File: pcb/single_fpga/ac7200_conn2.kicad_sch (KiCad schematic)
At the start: 1 part, among them U97 ALINX AC7200 (XC7A200T-2FBG48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

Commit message: Changed position.
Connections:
- net GND: now also U97.CON2_10 (GND), U97.CON2_19 (GND), U97.CON2_20 (GND), U97.CON2_29 (GND), U97.CON2_30 (GND), U97.CON2_39 (GND), U97.CON2_40 (GND), U97.CON2_49 (GND), U97.CON2_50 (GND), U97.CON2_59 (GND), U97.CON2_60 (GND), U97.CON2_69 (GND), U97.CON2_70 (GND), U97.CON2_9 (GND)

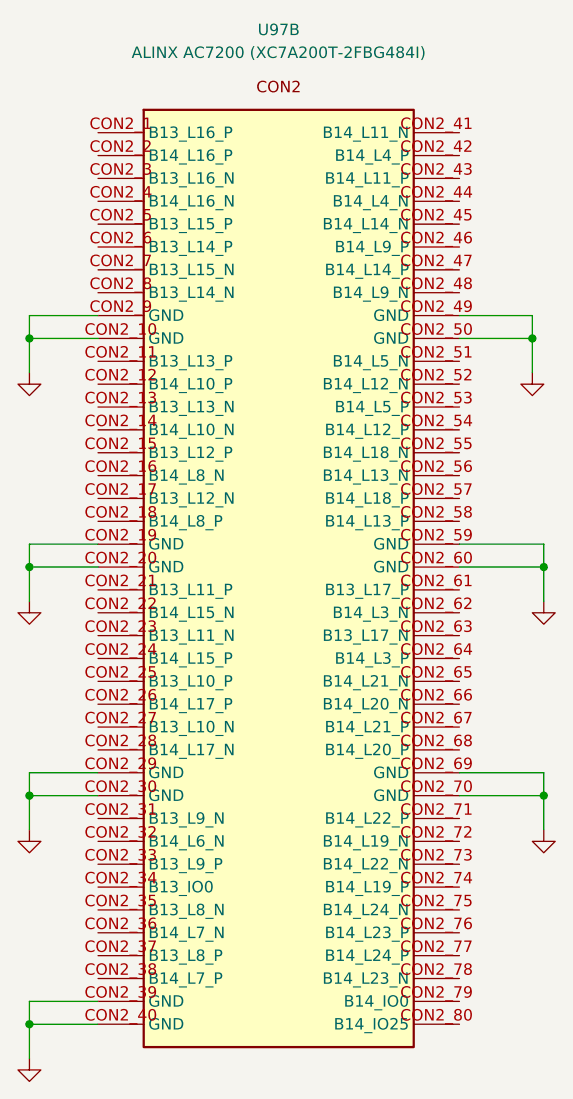
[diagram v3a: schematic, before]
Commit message: Reorganized sheets for two-boards. Fixed connector off-grid problems.
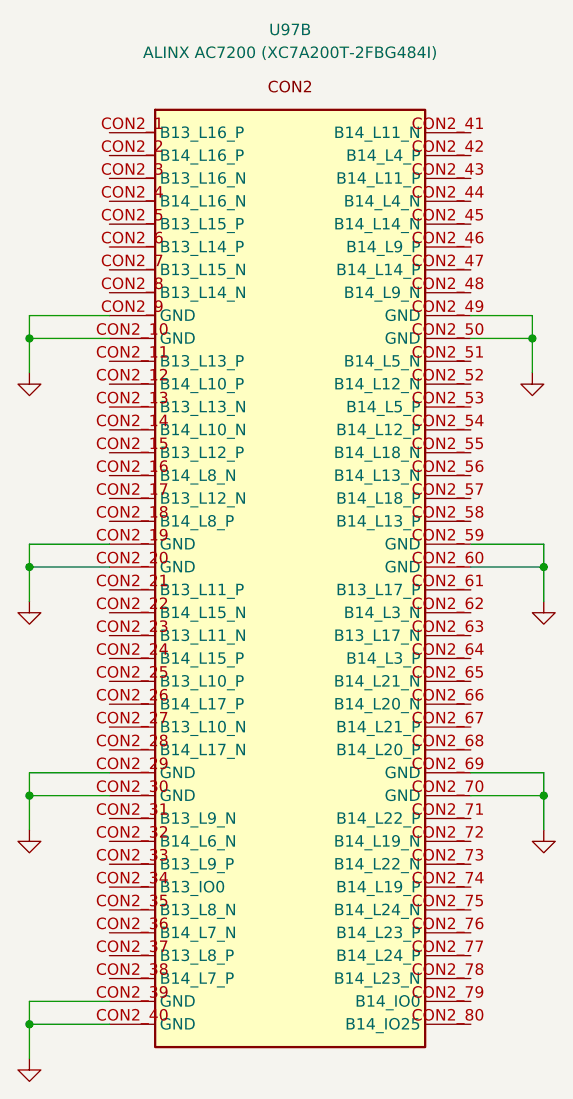
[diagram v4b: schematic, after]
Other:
- moved on the sheet: U97B
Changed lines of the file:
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@@
 	(paper "A4")
+	(junction
+		(at 114.3 101.6)
+		(diameter 0)
+		(color 0 0 0 0)
+	)
 	(junction
 		(at 114.3 127)
@@
 	)
 	(junction
-		(at 114.3 76.2)
+		(at 114.3 152.4)
 		(diameter 0)
 		(color 0 0 0 0)
@@
 	)
 	(junction
-		(at 114.3 152.4)
+		(at 170.18 76.2)
 		(diameter 0)
 		(color 0 0 0 0)
@@
 	)
 	(junction
-		(at 114.3 101.6)
+		(at 114.3 76.2)
 		(diameter 0)
 		(color 0 0 0 0)
 	)
-	(junction
-		(at 170.18 76.2)
-		(diameter 0)
-		(color 0 0 0 0)
-	)
-	(wire
-		(pts
-			(xy 162.08 101.6) (xy 171.45 101.6)
-		)
-		(stroke
-			(width 0)
-			(type default)
-		)
-	)
-	(wire
-		(pts
-			(xy 114.3 76.2) (xy 121.92 76.2)
-		)
-		(stroke
-			(width 0)
-			(type default)
-		)
-	)
-	(wire
-		(pts
-			(xy 162.08 73.66) (xy 170.18 73.66)
+	(wire
+		(pts
+			(xy 163.35 101.6) (xy 171.45 101.6)
+		)
+		(stroke
+			(width 0)
+			(type default)
+		)
+	)
+	(wire
+		(pts
+			(xy 114.3 76.2) (xy 123.19 76.2)
+		)
+		(stroke
+			(width 0)
+			(type default)
+		)
+	)
+	(wire
+		(pts
+			(xy 163.35 73.66) (xy 170.18 73.66)
 		)
 		(stroke
@@
 	(wire
 		(pts
-			(xy 114.3 99.06) (xy 121.92 99.06)
-		)
-		(stroke
-			(width 0)
-			(type default)
-		)
-	)
-	(wire
-		(pts
-			(xy 114.3 152.4) (xy 121.92 152.4)
+			(xy 114.3 99.06) (xy 123.19 99.06)
+		)
+		(stroke
+			(width 0)
+			(type default)
+		)
+	)
+	(wire
+		(pts
+			(xy 114.3 152.4) (xy 123.19 152.4)
 		)
 		(stroke
@@
 	(wire
 		(pts
-			(xy 162.08 124.46) (xy 171.45 124.46)
-		)
-		(stroke
-			(width 0)
-			(type default)
-		)
-	)
-	(wire
-		(pts
-			(xy 114.3 127) (xy 121.92 127)
-		)
-		(stroke
-			(width 0)
-			(type default)
-		)
-	)
-	(wire
-		(pts
-			(xy 162.08 99.06) (xy 171.45 99.06)
-		)
-		(stroke
-			(width 0)
-			(type default)
-		)
-	)
-	(wire
-		(pts
-			(xy 162.08 127) (xy 171.45 127)
+			(xy 163.35 124.46) (xy 171.45 124.46)
+		)
+		(stroke
+			(width 0)
+			(type default)
+		)
+	)
+	(wire
+		(pts
+			(xy 114.3 127) (xy 123.19 127)
+		)
+		(stroke
+			(width 0)
+			(type default)
+		)
+	)
+	(wire
+		(pts
+			(xy 163.35 99.06) (xy 171.45 99.06)
+		)
+		(stroke
+			(width 0)
+			(type default)
+		)
+	)
+	(wire
+		(pts
+			(xy 163.35 127) (xy 171.45 127)
 		)
 		(stroke
@@
 	(wire
 		(pts
-			(xy 114.3 73.66) (xy 121.92 73.66)
+			(xy 114.3 73.66) (xy 123.19 73.66)
 		)
 		(stroke
@@
 	(wire
 		(pts
-			(xy 114.3 149.86) (xy 121.92 149.86)
+			(xy 114.3 149.86) (xy 123.19 149.86)
 		)
 		(stroke
@@
 	(wire
 		(pts
-			(xy 162.08 76.2) (xy 170.18 76.2)
-		)
-		(stroke
-			(width 0)
-			(type default)
-		)
-	)
-	(wire
-		(pts
-			(xy 114.3 124.46) (xy 121.92 124.46)
+			(xy 163.35 76.2) (xy 170.18 76.2)
+		)
+		(stroke
+			(width 0)
+			(type default)
+		)
+	)
+	(wire
+		(pts
+			(xy 114.3 124.46) (xy 123.19 124.46)
 		)
 		(stroke
@@
 	(wire
 		(pts
-			(xy 114.3 101.6) (xy 121.92 101.6)
+			(xy 114.3 101.6) (xy 123.19 101.6)
 		)
 		(stroke
@@
 		(dnp no)
 		(fields_autoplaced yes)
-		(property "Reference" "#PWR009"
+		(property "Reference" "#PWR09"
 			(at 114.3 86.36 0)
 			(hide yes)
@@
 		(instances
 			(project "top"
-				(path "/12638caa-1907-413e-8e98-06abbbf6ccbc/d4107e22-3cf2-453c-a22c-8e2acaca2e5b/b8c40ea9-0d6a-4a7f-8d5e-85c23412f0d2"
-					(reference "#PWR009")
+				(path "/12638caa-1907-413e-8e98-06abbbf6ccbc/8ee3463b-0816-4e24-be6c-9811f4c49ad3/32c479b8-4af5-4d07-9387-f6769afc9e03"
+					(reference "#PWR09")
 					(unit 1)
 				)
@@
 	(symbol
 		(lib_id "single_fpga:AC7200")
-		(at 142 102.87 0)
+		(at 143.27 102.87 0)
 		(unit 2)
 		(body_style 1)
@@
 		(fields_autoplaced yes)
 		(property "Reference" "U97"
-			(at 142 41.91 0)
+			(at 143.27 41.91 0)
 			(show_name no)
 			(do_not_autoplace no)
@@
 		)
 		(property "Value" "ALINX AC7200 (XC7A200T-2FBG484I)"
-			(at 142 44.45 0)
+			(at 143.27 44.45 0)
 			(show_name no)
 			(do_not_autoplace no)
@@
 		)
 		(property "Footprint" "single_fpga:AC7200"
-			(at 142 102.87 0)
+			(at 143.27 102.87 0)
 			(hide yes)
 			(show_name no)
@@
 		)
 		(property "Datasheet" "docs/AC7200_User_Manual.pdf"
-			(at 142 102.87 0)
+			(at 143.27 102.87 0)
 			(hide yes)
 			(show_name no)
@@
 		)
 		(property "Description" "ALINX AC7200 XC7A200T-2FBG484I Artix-7 FPGA SOM, 45x55mm, 4x 80-pin/0.5mm B2B connectors (Unit A=CON1 VCCIN/GND+BANK34+BANK13+XADC, Unit B=CON2 BANK13+BANK14, Unit C=CON3 BANK15+BANK16+JTAG (TCK/TDI/TDO/TMS on pins 77-80 -- a SEPARATE on-module 6-pin JTAG header J1 also exists, not modeled here), Unit D=CON4 BANK16+GTP transceivers). Every pin cross-checked against ALINX's own real user manual (docs/AC7200_User_Manual.pdf) -- CON2/CON3/CON4 and CON1 pins 1-72 matched an earlier web-transcription exactly; CON1 pins 73-80 (previously unverified placeholder) now filled in from the real manual. ONE correction applied: CON1 pin 27 is printed as 'B13_L7_P' in ALINX's own manual (same as pin 25) -- a real duplicate/typo in their document (different FPGA balls AB11 vs AB12, and every other one of the 320 pins alternates P/N without exception) -- corrected here to B13_L7_N. Module standalone-power (J3, 2-pin +5V/GND) and JTAG (J1, 6-pin) headers exist on the module but are not part of this symbol (carrier-board-facing CON1-4 only)."
-			(at 142 102.87 0)
+			(at 143.27 102.87 0)
 			(hide yes)
 			(show_name no)
@@
 		(instances
 			(project "top"
-				(path "/12638caa-1907-413e-8e98-06abbbf6ccbc/d4107e22-3cf2-453c-a22c-8e2acaca2e5b/b8c40ea9-0d6a-4a7f-8d5e-85c23412f0d2"
+				(path "/12638caa-1907-413e-8e98-06abbbf6ccbc/8ee3463b-0816-4e24-be6c-9811f4c49ad3/32c479b8-4af5-4d07-9387-f6769afc9e03"
 					(reference "U97")
 					(unit 2)
@@
 		(instances
 			(project "top"
-				(path "/12638caa-1907-413e-8e98-06abbbf6ccbc/d4107e22-3cf2-453c-a22c-8e2acaca2e5b/b8c40ea9-0d6a-4a7f-8d5e-85c23412f0d2"
+				(path "/12638caa-1907-413e-8e98-06abbbf6ccbc/8ee3463b-0816-4e24-be6c-9811f4c49ad3/32c479b8-4af5-4d07-9387-f6769afc9e03"
 					(reference "#PWR010")
 					(unit 1)
@@
 		(instances
 			(project "top"
-				(path "/12638caa-1907-413e-8e98-06abbbf6ccbc/d4107e22-3cf2-453c-a22c-8e2acaca2e5b/b8c40ea9-0d6a-4a7f-8d5e-85c23412f0d2"
+				(path "/12638caa-1907-413e-8e98-06abbbf6ccbc/8ee3463b-0816-4e24-be6c-9811f4c49ad3/32c479b8-4af5-4d07-9387-f6769afc9e03"
 					(reference "#PWR011")
 					(unit 1)
@@
 		(instances
 			(project "top"
-				(path "/12638caa-1907-413e-8e98-06abbbf6ccbc/d4107e22-3cf2-453c-a22c-8e2acaca2e5b/b8c40ea9-0d6a-4a7f-8d5e-85c23412f0d2"
+				(path "/12638caa-1907-413e-8e98-06abbbf6ccbc/8ee3463b-0816-4e24-be6c-9811f4c49ad3/32c479b8-4af5-4d07-9387-f6769afc9e03"
 					(reference "#PWR012")
 					(unit 1)
@@
 		(instances
 			(project "top"
-				(path "/12638caa-1907-413e-8e98-06abbbf6ccbc/d4107e22-3cf2-453c-a22c-8e2acaca2e5b/b8c40ea9-0d6a-4a7f-8d5e-85c23412f0d2"
+				(path "/12638caa-1907-413e-8e98-06abbbf6ccbc/8ee3463b-0816-4e24-be6c-9811f4c49ad3/32c479b8-4af5-4d07-9387-f6769afc9e03"
 					(reference "#PWR013")
 					(unit 1)
@@
 		(instances
 			(project "top"
-				(path "/12638caa-1907-413e-8e98-06abbbf6ccbc/d4107e22-3cf2-453c-a22c-8e2acaca2e5b/b8c40ea9-0d6a-4a7f-8d5e-85c23412f0d2"
+				(path "/12638caa-1907-413e-8e98-06abbbf6ccbc/8ee3463b-0816-4e24-be6c-9811f4c49ad3/32c479b8-4af5-4d07-9387-f6769afc9e03"
 					(reference "#PWR014")
 					(unit 1)
@@
 		(instances
 			(project "top"
-				(path "/12638caa-1907-413e-8e98-06abbbf6ccbc/d4107e22-3cf2-453c-a22c-8e2acaca2e5b/b8c40ea9-0d6a-4a7f-8d5e-85c23412f0d2"
+				(path "/12638caa-1907-413e-8e98-06abbbf6ccbc/8ee3463b-0816-4e24-be6c-9811f4c49ad3/32c479b8-4af5-4d07-9387-f6769afc9e03"
 					(reference "#PWR015")
 					(unit 1)

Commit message: Fixed another off-grid issue. Connected power and DATA_?? pins to inter-board connector.
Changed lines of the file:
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@@
 	(wire
 		(pts
-			(xy 163.35 101.6) (xy 171.45 101.6)
+			(xy 163.83 76.2) (xy 170.18 76.2)
 		)
 		(stroke
@@
 	(wire
 		(pts
-			(xy 163.35 73.66) (xy 170.18 73.66)
+			(xy 163.83 99.06) (xy 171.45 99.06)
 		)
 		(stroke
@@
 	(wire
 		(pts
+			(xy 163.83 73.66) (xy 170.18 73.66)
+		)
+		(stroke
+			(width 0)
+			(type default)
+		)
+	)
+	(wire
+		(pts
 			(xy 114.3 99.06) (xy 114.3 101.6)
 		)
@@
 	(wire
 		(pts
+			(xy 163.83 124.46) (xy 171.45 124.46)
+		)
+		(stroke
+			(width 0)
+			(type default)
+		)
+	)
+	(wire
+		(pts
 			(xy 114.3 152.4) (xy 123.19 152.4)
 		)
@@
 	(wire
 		(pts
-			(xy 163.35 124.46) (xy 171.45 124.46)
-		)
-		(stroke
-			(width 0)
-			(type default)
-		)
-	)
-	(wire
-		(pts
 			(xy 114.3 127) (xy 123.19 127)
 		)
@@
 	(wire
 		(pts
-			(xy 163.35 99.06) (xy 171.45 99.06)
-		)
-		(stroke
-			(width 0)
-			(type default)
-		)
-	)
-	(wire
-		(pts
-			(xy 163.35 127) (xy 171.45 127)
-		)
-		(stroke
-			(width 0)
-			(type default)
-		)
-	)
-	(wire
-		(pts
 			(xy 171.45 127) (xy 171.45 130.81)
 		)
@@
 	(wire
 		(pts
+			(xy 163.83 101.6) (xy 171.45 101.6)
+		)
+		(stroke
+			(width 0)
+			(type default)
+		)
+	)
+	(wire
+		(pts
+			(xy 163.83 127) (xy 171.45 127)
+		)
+		(stroke
+			(width 0)
+			(type default)
+		)
+	)
+	(wire
+		(pts
 			(xy 171.45 124.46) (xy 171.45 127)
-		)
-		(stroke
-			(width 0)
-			(type default)
-		)
-	)
-	(wire
-		(pts
-			(xy 163.35 76.2) (xy 170.18 76.2)
 		)
 		(stroke
@@
 	(symbol
 		(lib_id "single_fpga:AC7200")
-		(at 143.27 102.87 0)
+		(at 143.51 102.87 0)
 		(unit 2)
 		(body_style 1)
@@
 		(fields_autoplaced yes)
 		(property "Reference" "U97"
-			(at 143.27 41.91 0)
+			(at 143.51 41.91 0)
 			(show_name no)
 			(do_not_autoplace no)
@@
 		)
 		(property "Value" "ALINX AC7200 (XC7A200T-2FBG484I)"
-			(at 143.27 44.45 0)
+			(at 143.51 44.45 0)
 			(show_name no)
 			(do_not_autoplace no)
@@
 		)
 		(property "Footprint" "single_fpga:AC7200"
-			(at 143.27 102.87 0)
+			(at 143.51 102.87 0)
 			(hide yes)
 			(show_name no)
@@
 		)
 		(property "Datasheet" "docs/AC7200_User_Manual.pdf"
-			(at 143.27 102.87 0)
+			(at 143.51 102.87 0)
 			(hide yes)
 			(show_name no)
@@
 		)
 		(property "Description" "ALINX AC7200 XC7A200T-2FBG484I Artix-7 FPGA SOM, 45x55mm, 4x 80-pin/0.5mm B2B connectors (Unit A=CON1 VCCIN/GND+BANK34+BANK13+XADC, Unit B=CON2 BANK13+BANK14, Unit C=CON3 BANK15+BANK16+JTAG (TCK/TDI/TDO/TMS on pins 77-80 -- a SEPARATE on-module 6-pin JTAG header J1 also exists, not modeled here), Unit D=CON4 BANK16+GTP transceivers). Every pin cross-checked against ALINX's own real user manual (docs/AC7200_User_Manual.pdf) -- CON2/CON3/CON4 and CON1 pins 1-72 matched an earlier web-transcription exactly; CON1 pins 73-80 (previously unverified placeholder) now filled in from the real manual. ONE correction applied: CON1 pin 27 is printed as 'B13_L7_P' in ALINX's own manual (same as pin 25) -- a real duplicate/typo in their document (different FPGA balls AB11 vs AB12, and every other one of the 320 pins alternates P/N without exception) -- corrected here to B13_L7_N. Module standalone-power (J3, 2-pin +5V/GND) and JTAG (J1, 6-pin) headers exist on the module but are not part of this symbol (carrier-board-facing CON1-4 only)."
-			(at 143.27 102.87 0)
-			(hide yes)
-			(show_name no)
+			(at 143.51 102.87 0)
+			(hide yes)
+			(show_name no)

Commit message: Updated all refdes's.
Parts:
- renumbered U97 to U109
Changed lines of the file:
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@@
 		(dnp no)
 		(fields_autoplaced yes)
-		(property "Reference" "#PWR09"
+		(property "Reference" "#PWR0438"
 			(at 114.3 86.36 0)
 			(hide yes)
@@
 			(project "top"
 				(path "/12638caa-1907-413e-8e98-06abbbf6ccbc/8ee3463b-0816-4e24-be6c-9811f4c49ad3/32c479b8-4af5-4d07-9387-f6769afc9e03"
-					(reference "#PWR09")
+					(reference "#PWR0438")
 					(unit 1)
 				)
@@
 		(dnp no)
 		(fields_autoplaced yes)
-		(property "Reference" "U97"
+		(property "Reference" "U109"
 			(at 143.51 41.91 0)
 			(show_name no)
@@
 			(project "top"
 				(path "/12638caa-1907-413e-8e98-06abbbf6ccbc/8ee3463b-0816-4e24-be6c-9811f4c49ad3/32c479b8-4af5-4d07-9387-f6769afc9e03"
-					(reference "U97")
+					(reference "U109")
 					(unit 2)
 				)
@@
 		(dnp no)
 		(fields_autoplaced yes)
-		(property "Reference" "#PWR010"
+		(property "Reference" "#PWR0444"
 			(at 171.45 137.16 0)
 			(hide yes)
@@
 			(project "top"
 				(path "/12638caa-1907-413e-8e98-06abbbf6ccbc/8ee3463b-0816-4e24-be6c-9811f4c49ad3/32c479b8-4af5-4d07-9387-f6769afc9e03"
-					(reference "#PWR010")
+					(reference "#PWR0444")
 					(unit 1)
 				)
@@
 		(dnp no)
 		(fields_autoplaced yes)
-		(property "Reference" "#PWR011"
+		(property "Reference" "#PWR0441"
 			(at 114.3 162.56 0)
 			(hide yes)
@@
 			(project "top"
 				(path "/12638caa-1907-413e-8e98-06abbbf6ccbc/8ee3463b-0816-4e24-be6c-9811f4c49ad3/32c479b8-4af5-4d07-9387-f6769afc9e03"
-					(reference "#PWR011")
+					(reference "#PWR0441")
 					(unit 1)
 				)
@@
 		(dnp no)
 		(fields_autoplaced yes)
-		(property "Reference" "#PWR012"
+		(property "Reference" "#PWR0439"
 			(at 114.3 111.76 0)
 			(hide yes)
@@
 			(project "top"
 				(path "/12638caa-1907-413e-8e98-06abbbf6ccbc/8ee3463b-0816-4e24-be6c-9811f4c49ad3/32c479b8-4af5-4d07-9387-f6769afc9e03"
-					(reference "#PWR012")
+					(reference "#PWR0439")
 					(unit 1)
 				)
@@
 		(dnp no)
 		(fields_autoplaced yes)
-		(property "Reference" "#PWR013"
+		(property "Reference" "#PWR0442"
 			(at 170.18 86.36 0)
 			(hide yes)
@@
 			(project "top"
 				(path "/12638caa-1907-413e-8e98-06abbbf6ccbc/8ee3463b-0816-4e24-be6c-9811f4c49ad3/32c479b8-4af5-4d07-9387-f6769afc9e03"
-					(reference "#PWR013")
+					(reference "#PWR0442")
 					(unit 1)
 				)
@@
 		(dnp no)
 		(fields_autoplaced yes)
-		(property "Reference" "#PWR014"
+		(property "Reference" "#PWR0443"
 			(at 171.45 111.76 0)
 			(hide yes)
@@
 			(project "top"
 				(path "/12638caa-1907-413e-8e98-06abbbf6ccbc/8ee3463b-0816-4e24-be6c-9811f4c49ad3/32c479b8-4af5-4d07-9387-f6769afc9e03"
-					(reference "#PWR014")
+					(reference "#PWR0443")
 					(unit 1)
 				)
@@
 		(dnp no)
 		(fields_autoplaced yes)
-		(property "Reference" "#PWR015"
+		(property "Reference" "#PWR0440"
 			(at 114.3 137.16 0)
 			(hide yes)
@@
 			(project "top"
 				(path "/12638caa-1907-413e-8e98-06abbbf6ccbc/8ee3463b-0816-4e24-be6c-9811f4c49ad3/32c479b8-4af5-4d07-9387-f6769afc9e03"
-					(reference "#PWR015")
+					(reference "#PWR0440")
 					(unit 1)
 				)

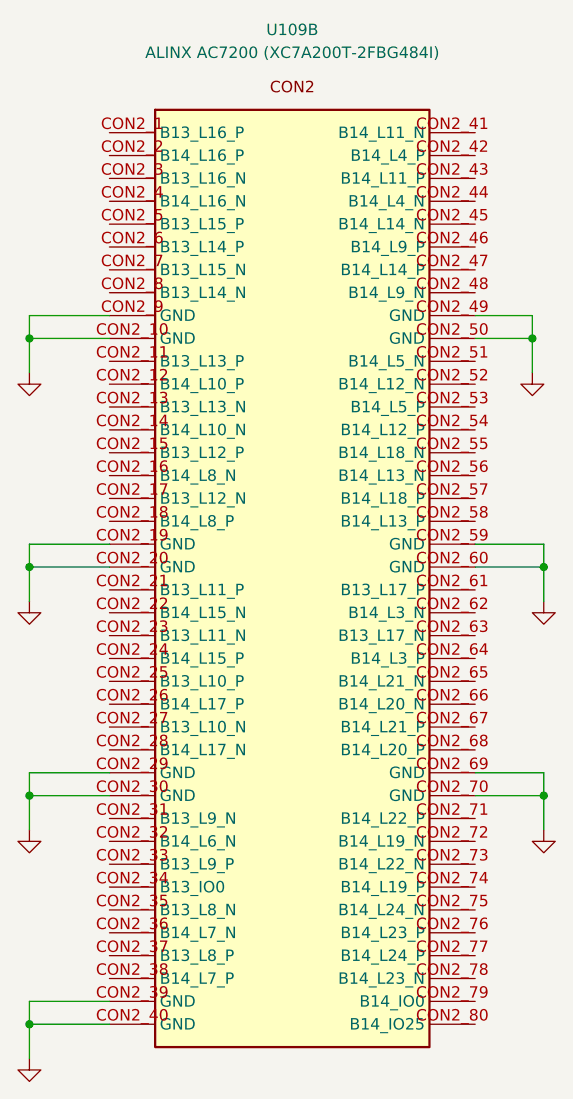
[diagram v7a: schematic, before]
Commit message: Added Ethernet interface. Fixed power rails. ERC-clean.
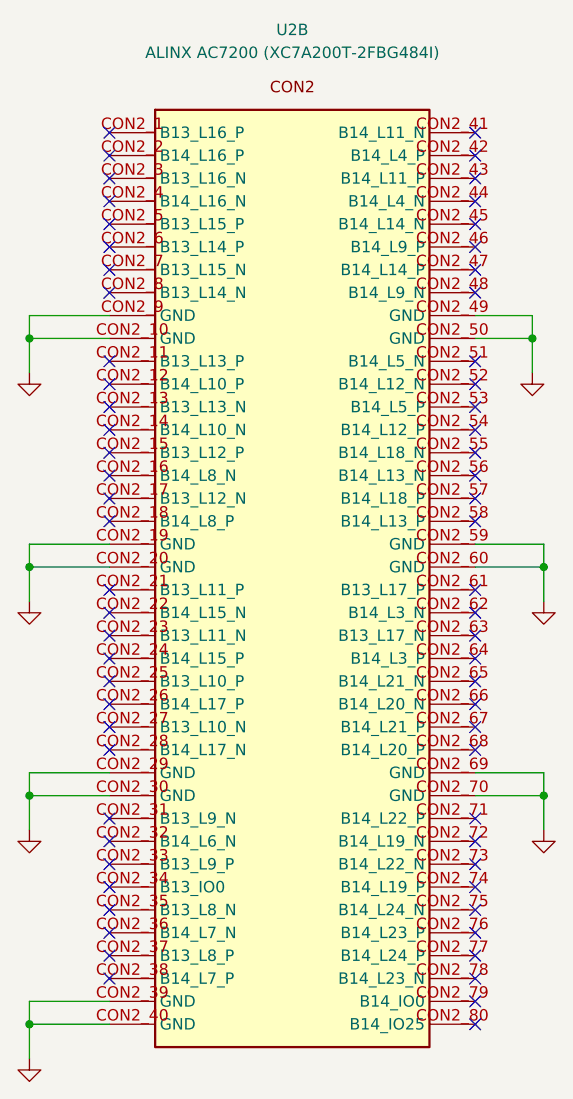
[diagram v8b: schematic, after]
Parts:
- renumbered U109 to U2
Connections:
- no-connect marks 0 -> 66
